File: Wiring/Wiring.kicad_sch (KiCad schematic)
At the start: 3 parts

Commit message: chore: add author, licensce and GitHub repository info
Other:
- company: (none) -> Ozonised
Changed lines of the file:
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@@
 		(title "Signal Node Wiring")
 		(date "2024-09-08")
+		(company "Ozonised")
+		(comment 2 "License: GNU General Public License version 3")
+		(comment 3 "GitHub: https://github.com/Ozonised/OTAPS_Hardware")
+		(comment 4 "Author: Farhan Khan")
 	)
 	(junction

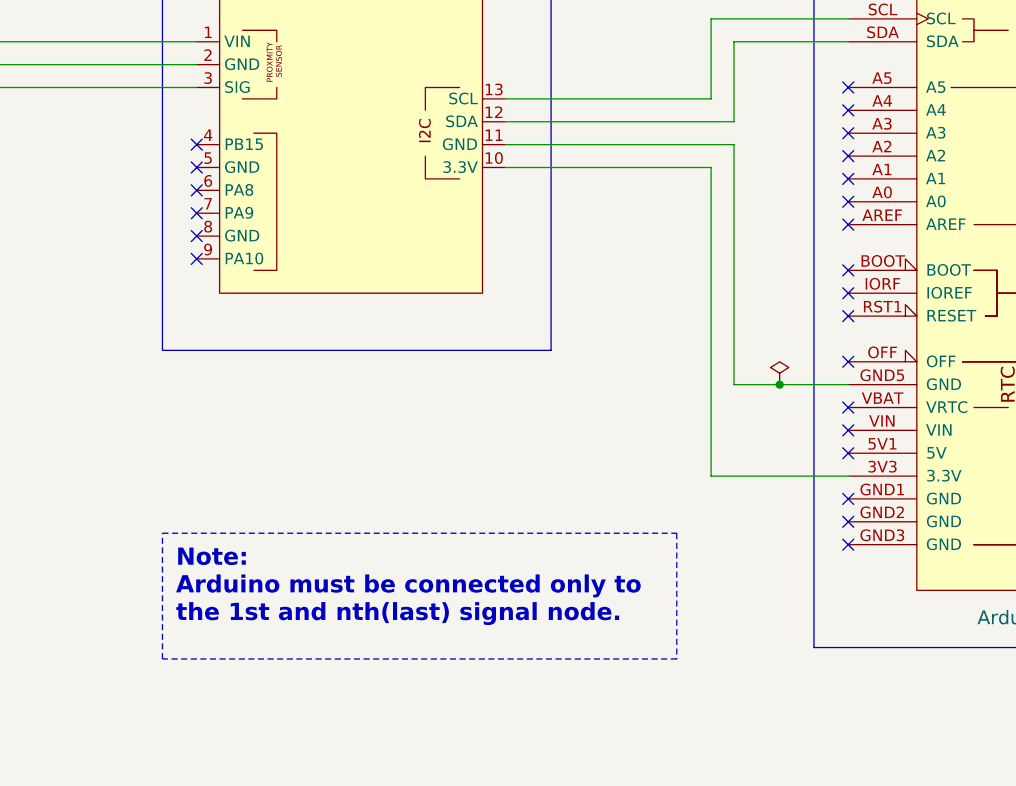
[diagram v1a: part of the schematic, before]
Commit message: fix: remove 3.3V connection between arduino & signal node
The signal node and the arduino should be powered from the barrel connector.
Also added a note regarding this to the schematic.
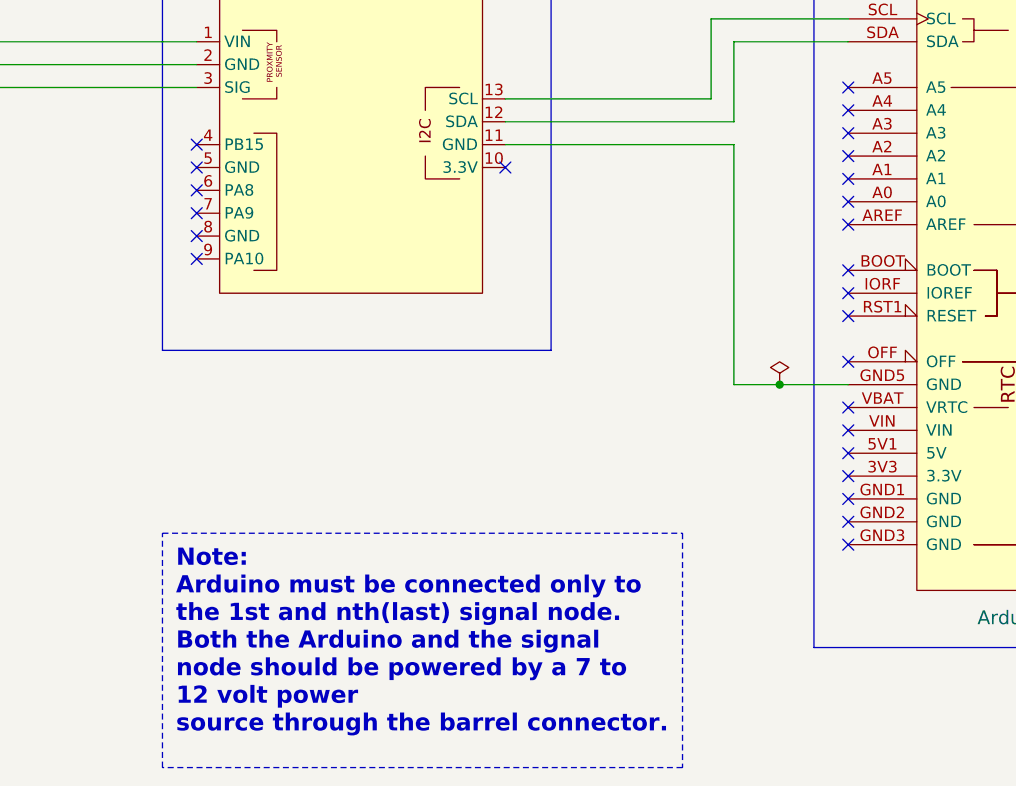
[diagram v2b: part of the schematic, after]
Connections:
- net at A1.3V3 (3.3V): no longer U1.10 (3.3V)
- no-connect marks 49 -> 51
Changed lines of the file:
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@@
+	)
+	(no_connect
+		(at 157.48 95.25)
 	)
 	(no_connect
@@
 		(at 246.38 132.08)
 	)
+	(no_connect
+		(at 195.58 129.54)
+	)
 	(wire
 		(pts
@@
 		(pts
 			(xy 180.34 87.63) (xy 157.48 87.63)
-		)
-		(stroke
-			(width 0)
-			(type default)
-		)
-	)
-	(wire
-		(pts
-			(xy 180.34 95.25) (xy 157.48 95.25)
-		)
-		(stroke
-			(width 0)
-			(type default)
-		)
-	)
-	(wire
-		(pts
-			(xy 195.58 129.54) (xy 180.34 129.54)
-		)
-		(stroke
-			(width 0)
-			(type default)
-		)
-	)
-	(wire
-		(pts
-			(xy 180.34 129.54) (xy 180.34 95.25)
 		)
 		(stroke
@@
 		)
 	)
-	(text_box "Note:\nArduino must be connected only to the 1st and nth(last) signal node. \n"
+	(text_box "Note:\nArduino must be connected only to the 1st and nth(last) signal node.\nBoth the Arduino and the signal node should be powered by a 7 to 12 volt power\nsource through the barrel connector.\n"
 		(exclude_from_sim no)
 		(at 119.38 135.89 0)
-		(size 57.15 13.97)
+		(size 57.785 26.035)
 		(stroke
 			(width 0.1016)
